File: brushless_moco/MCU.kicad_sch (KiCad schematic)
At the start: 0 parts

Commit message: Added can transciever and current sensor symbols and libraries
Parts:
- added IC1: TLT9251VLEXUMA1, brushless_moco_footprints:SON65P300X300X110-9N, symbol brushless_moco_symbols:TLT9251VLEXUMA1
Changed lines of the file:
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@@
 	(generator_version "9.0")
 	(paper "A4")
+	(symbol
+		(lib_id "brushless_moco_symbols:TLT9251VLEXUMA1")
+		(at 73.66 111.76 0)
+		(unit 1)
+		(exclude_from_sim no)
+		(in_bom yes)
+		(on_board yes)
+		(dnp no)
+		(fields_autoplaced yes)
+		(property "Reference" "IC1"
+			(at 88.9 104.14 0)
+			(effects
+				(font
+					(size 1.27 1.27)
+				)
+			)
+		)
+		(property "Value" "TLT9251VLEXUMA1"
+			(at 88.9 106.68 0)
+			(effects
+				(font
+					(size 1.27 1.27)
+				)
+			)
+		)
+		(property "Footprint" "brushless_moco_footprints:SON65P300X300X110-9N"
+			(at 100.33 206.68 0)
+			(effects
+				(font
+					(size 1.27 1.27)
+				)
+				(justify left top)
+				(hide yes)
+			)
+		)
+		(property "Datasheet" "https://www.infineon.com/dgdl/Infineon-TLT9251VLE-DataSheet-v01_00-EN.pdf?fileId=5546d4626e8d4b8f016ea702cfff08e8"
+			(at 100.33 306.68 0)
+			(effects
+				(font
+					(size 1.27 1.27)
+				)
+				(justify left top)
+				(hide yes)
+			)
+		)
+		(property "Description" "CAN Interface IC"
+			(at 73.66 111.76 0)
+			(effects
+				(font
+					(size 1.27 1.27)
+				)
+				(hide yes)
+			)
+		)
+		(property "Height" "1.1"
+			(at 100.33 506.68 0)
+			(effects
+				(font
+					(size 1.27 1.27)
+				)
+				(justify left top)
+				(hide yes)
+			)
+		)
+		(property "Manufacturer_Name" "Infineon"
+			(at 100.33 606.68 0)
+			(effects
+				(font
+					(size 1.27 1.27)
+				)
+				(justify left top)
+				(hide yes)
+			)
+		)
+		(property "Manufacturer_Part_Number" "TLT9251VLEXUMA1"
+			(at 100.33 706.68 0)
+			(effects
+				(font
+					(size 1.27 1.27)
+				)
+				(justify left top)
+				(hide yes)
+			)
+		)
+		(property "Mouser Part Number" "726-TLT9251VLEXUMA1"
+			(at 100.33 806.68 0)
+			(effects
+				(font
+					(size 1.27 1.27)
+				)
+				(justify left top)
+				(hide yes)
+			)
+		)
+		(property "Mouser Price/Stock" "https://www.mouser.co.uk/ProductDetail/Infineon-Technologies/TLT9251VLEXUMA1?qs=W%2FMpXkg%252BdQ5zGtp9sfvtfA%3D%3D"
+			(at 100.33 906.68 0)
+			(effects
+				(font
+					(size 1.27 1.27)
+				)
+				(justify left top)
+				(hide yes)
+			)
+		)
+		(property "Arrow Part Number" "TLT9251VLEXUMA1"
+			(at 100.33 1006.68 0)
+			(effects
+				(font
+					(size 1.27 1.27)
+				)
+				(justify left top)
+				(hide yes)
+			)
+		)
+		(property "Arrow Price/Stock" "https://www.arrow.com/en/products/tlt9251vlexuma1/infineon-technologies-ag?region=nac"
+			(at 100.33 1106.68 0)
+			(effects
+				(font
+					(size 1.27 1.27)
+				)
+				(justify left top)
+				(hide yes)
+			)
+		)
+		(pin "1"
+		)
+		(pin "2"
+		)
+		(pin "7"
+		)
+		(pin "6"
+		)
+		(pin "3"
+		)
+		(pin "4"
+		)
+		(pin "9"
+		)
+		(pin "8"
+		)
+		(pin "5"
+		)
+		(instances
+			(project ""
+				(path "/1ef8bc88-f0df-4a97-862b-c4b9ec3b4ed0/02edeb2f-867a-4e66-ac0c-df2434256428"
+					(reference "IC1")
+					(unit 1)
+				)
+			)
+		)
+	)
 )

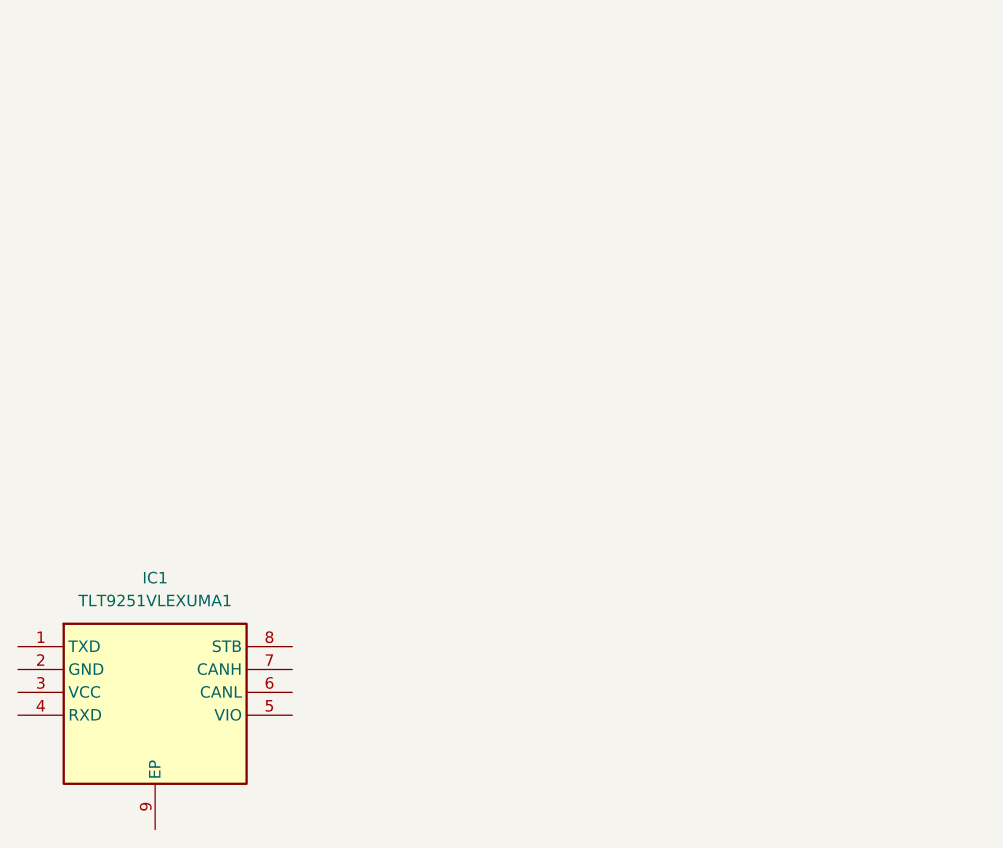
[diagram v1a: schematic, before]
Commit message: Added kicad workflow
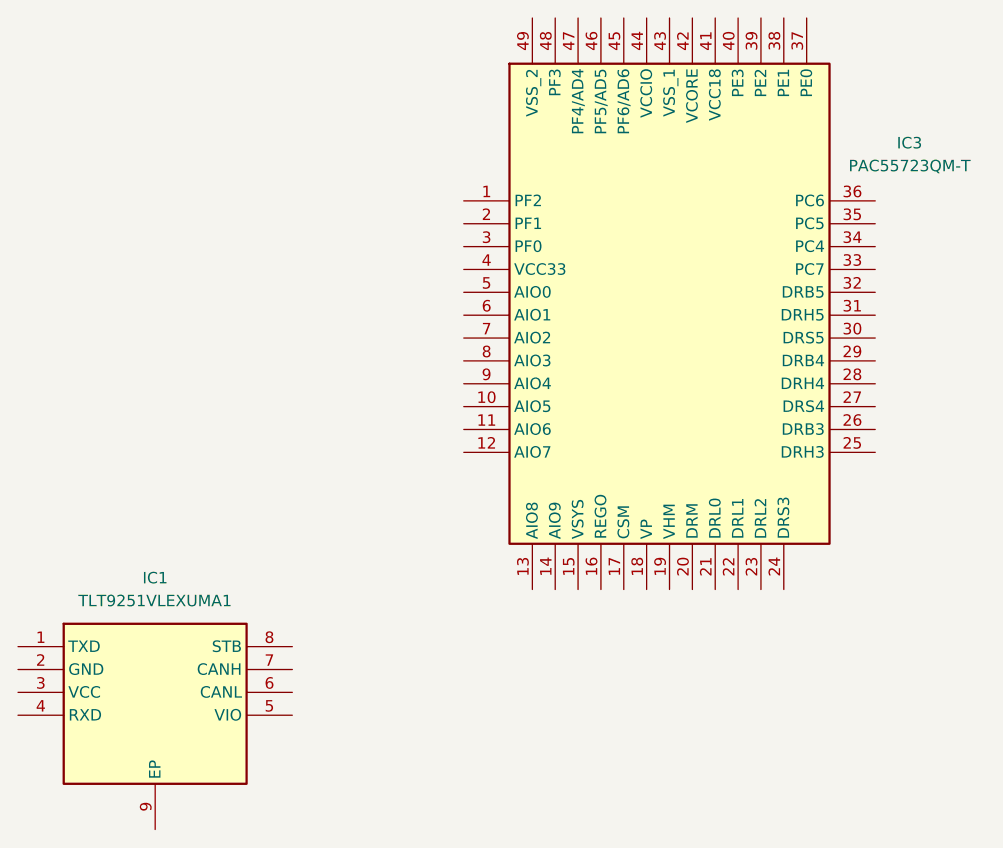
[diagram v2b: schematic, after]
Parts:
- added IC3: PAC55723QM-T, brushless_moco_footprints:QFN40P600X600X80-49N-D, symbol brushless_moco_symbols:PAC55723QM-T
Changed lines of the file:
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@@
+		)
+	)
+	(symbol
+		(lib_id "brushless_moco_symbols:PAC55723QM-T")
+		(at 123.19 62.23 0)
+		(unit 1)
+		(exclude_from_sim no)
+		(in_bom yes)
+		(on_board yes)
+		(dnp no)
+		(fields_autoplaced yes)
+		(property "Reference" "IC3"
+			(at 172.72 55.8098 0)
+			(effects
+				(font
+					(size 1.27 1.27)
+				)
+			)
+		)
+		(property "Value" "PAC55723QM-T"
+			(at 172.72 58.3498 0)
+			(effects
+				(font
+					(size 1.27 1.27)
+				)
+			)
+		)
+		(property "Footprint" "brushless_moco_footprints:QFN40P600X600X80-49N-D"
+			(at 165.1 144.45 0)
+			(effects
+				(font
+					(size 1.27 1.27)
+				)
+				(justify left top)
+				(hide yes)
+			)
+		)
+		(property "Datasheet" "https://www.qorvo.com/products/d/da009271"
+			(at 165.1 244.45 0)
+			(effects
+				(font
+					(size 1.27 1.27)
+				)
+				(justify left top)
+				(hide yes)
+			)
+		)
+		(property "Description" "70 Volt BLDC Motor Controller & Driver with Advanced Production Features"
+			(at 123.19 62.23 0)
+			(effects
+				(font
+					(size 1.27 1.27)
+				)
+				(hide yes)
+			)
+		)
+		(property "Height" "0.8"
+			(at 165.1 444.45 0)
+			(effects
+				(font
+					(size 1.27 1.27)
+				)
+				(justify left top)
+				(hide yes)
+			)
+		)
+		(property "Manufacturer_Name" "Qorvo"
+			(at 165.1 544.45 0)
+			(effects
+				(font
+					(size 1.27 1.27)
+				)
+				(justify left top)
+				(hide yes)
+			)
+		)
+		(property "Manufacturer_Part_Number" "PAC55723QM-T"
+			(at 165.1 644.45 0)
+			(effects
+				(font
+					(size 1.27 1.27)
+				)
+				(justify left top)
+				(hide yes)
+			)
+		)
+		(property "Mouser Part Number" ""
+			(at 165.1 744.45 0)
+			(effects
+				(font
+					(size 1.27 1.27)
+				)
+				(justify left top)
+				(hide yes)
+			)
+		)
+		(property "Mouser Price/Stock" ""
+			(at 165.1 844.45 0)
+			(effects
+				(font
+					(size 1.27 1.27)
+				)
+				(justify left top)
+				(hide yes)
+			)
+		)
+		(property "Arrow Part Number" ""
+			(at 165.1 944.45 0)
+			(effects
+				(font
+					(size 1.27 1.27)
+				)
+				(justify left top)
+				(hide yes)
+			)
+		)
+		(property "Arrow Price/Stock" ""
+			(at 165.1 1044.45 0)
+			(effects
+				(font
+					(size 1.27 1.27)
+				)
+				(justify left top)
+				(hide yes)
+			)
+		)
+		(pin "5"
+		)
+		(pin "46"
+		)
+		(pin "17"
+		)
+		(pin "43"
+		)
+		(pin "9"
+		)
+		(pin "11"
+		)
+		(pin "48"
+		)
+		(pin "45"
+		)
+		(pin "8"
+		)
+		(pin "22"
+		)
+		(pin "23"
+		)
+		(pin "24"
+		)
+		(pin "15"
+		)
+		(pin "10"
+		)
+		(pin "44"
+		)
+		(pin "6"
+		)
+		(pin "4"
+		)
+		(pin "12"
+		)
+		(pin "13"
+		)
+		(pin "7"
+		)
+		(pin "49"
+		)
+		(pin "3"
+		)
+		(pin "47"
+		)
+		(pin "1"
+		)
+		(pin "2"
+		)
+		(pin "14"
+		)
+		(pin "16"
+		)
+		(pin "18"
+		)
+		(pin "19"
+		)
+		(pin "42"
+		)
+		(pin "20"
+		)
+		(pin "41"
+		)
+		(pin "21"
+		)
+		(pin "40"
+		)
+		(pin "39"
+		)
+		(pin "38"
+		)
+		(pin "32"
+		)
+		(pin "29"
+		)
+		(pin "36"
+		)
+		(pin "28"
+		)
+		(pin "27"
+		)
+		(pin "25"
+		)
+		(pin "26"
+		)
+		(pin "35"
+		)
+		(pin "34"
+		)
+		(pin "33"
+		)
+		(pin "30"
+		)
+		(pin "37"
+		)
+		(pin "31"
+		)
+		(instances
+			(project ""
+				(path "/1ef8bc88-f0df-4a97-862b-c4b9ec3b4ed0/02edeb2f-867a-4e66-ac0c-df2434256428"
+					(reference "IC3")
+					(unit 1)
+				)
+			)
 		)
 	)
